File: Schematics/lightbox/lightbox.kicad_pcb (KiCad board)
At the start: 2 copper layers, 51 x 62 mm, 25 parts, among them J1 Screw_Terminal_01x04, J2 Conn_01x11_Female, J3 Conn_01x07_Female, J4 Conn_02x03_Odd_Even, Q1 IRF530, Q2 IRF530, U1 74AHCT595, U2 74HC595, U3 ATtiny85-20P, U4 LM317_TO-220

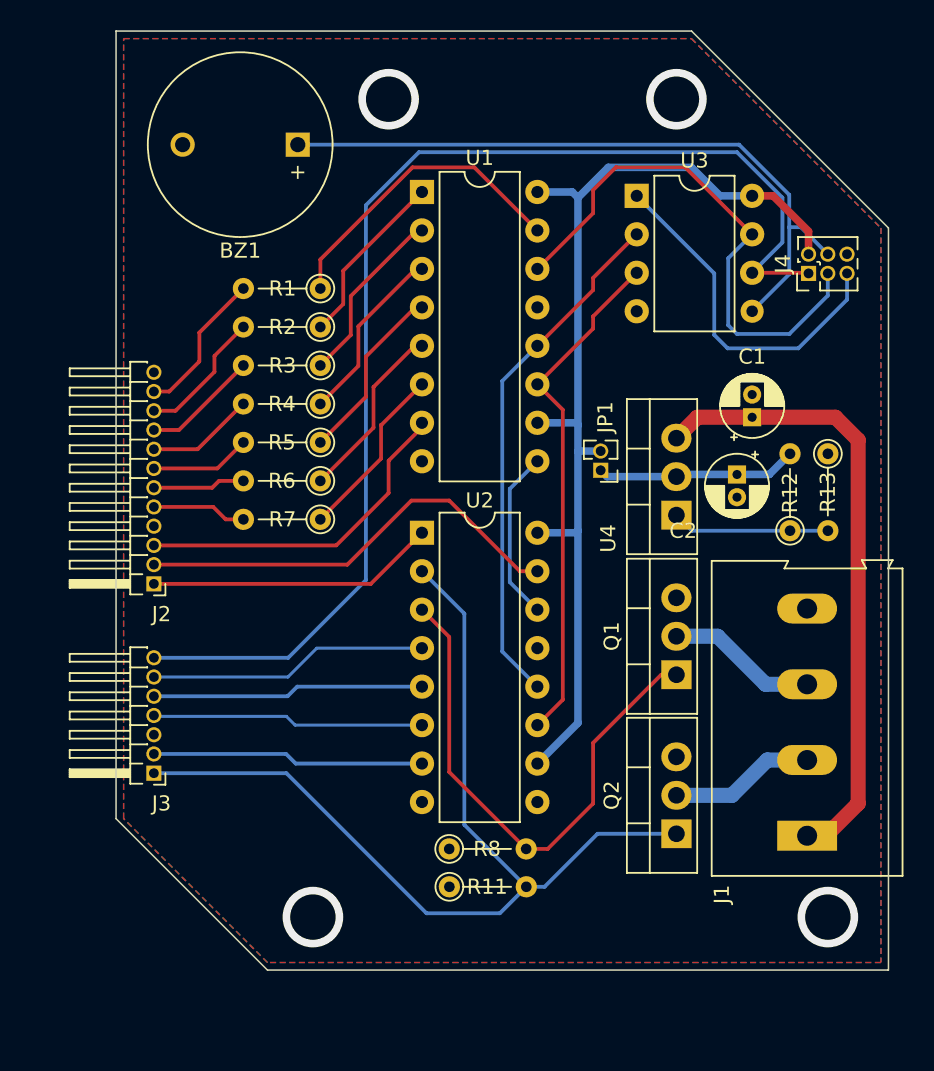
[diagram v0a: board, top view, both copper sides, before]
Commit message: Update lightbox design
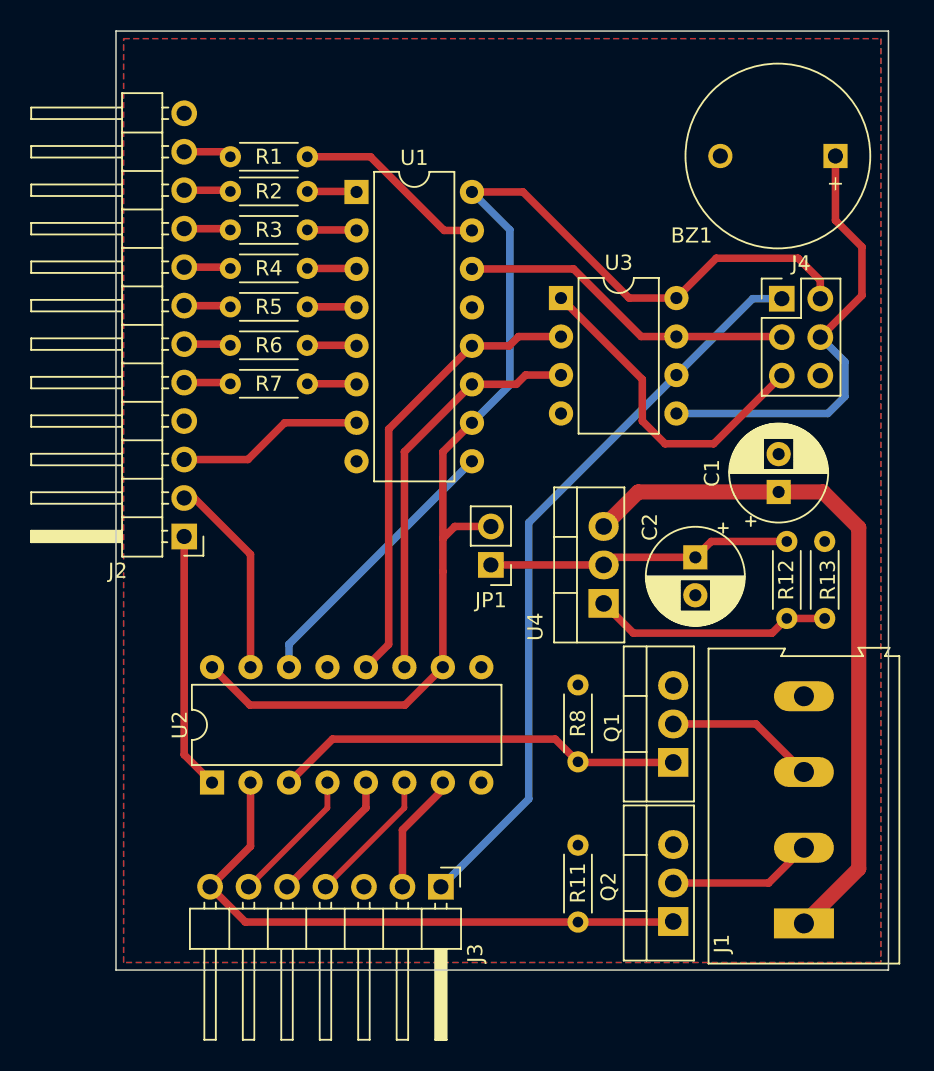
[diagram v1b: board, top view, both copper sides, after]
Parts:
- C1: value 0.1µF -> 100nF; footprint Capacitor_THT:CP_Radial_D4.0mm_P1.50mm -> Capacitor_THT:CP_Radial_D6.3mm_P2.50mm
- C2: value 10µF -> 1µF; footprint Capacitor_THT:CP_Radial_D4.0mm_P1.50mm -> Capacitor_THT:CP_Radial_D6.3mm_P2.50mm
- J2: value Conn_01x11_Female -> Conn_01x11_Pin; footprint Connector_PinHeader_1.27mm:PinHeader_1x12_P1.27mm_Horizontal -> Connector_PinHeader_2.54mm:PinHeader_1x12_P2.54mm_Horizontal
- J3: value Conn_01x07_Female -> Conn_01x07_Pin; footprint Connector_PinHeader_1.27mm:PinHeader_1x07_P1.27mm_Horizontal -> Connector_PinHeader_2.54mm:PinHeader_1x07_P2.54mm_Horizontal
- J4: footprint Connector_PinHeader_1.27mm:PinHeader_2x03_P1.27mm_Vertical -> Connector_PinHeader_2.54mm:PinHeader_2x03_P2.54mm_Vertical
- JP1: footprint Connector_PinHeader_1.27mm:PinHeader_1x02_P1.27mm_Vertical -> Connector_PinHeader_2.54mm:PinHeader_1x02_P2.54mm_Vertical
- R1, R11, R2, R3, R4, R5, R6, R7, R8: footprint Resistor_THT:R_Axial_DIN0204_L3.6mm_D1.6mm_P5.08mm_Vertical -> Resistor_THT:R_Axial_DIN0204_L3.6mm_D1.6mm_P5.08mm_Horizontal
- R12: value 100 -> 100R; footprint Resistor_THT:R_Axial_DIN0204_L3.6mm_D1.6mm_P5.08mm_Vertical -> Resistor_THT:R_Axial_DIN0204_L3.6mm_D1.6mm_P5.08mm_Horizontal
- R13: value 220 -> 220R; footprint Resistor_THT:R_Axial_DIN0204_L3.6mm_D1.6mm_P5.08mm_Vertical -> Resistor_THT:R_Axial_DIN0204_L3.6mm_D1.6mm_P5.08mm_Horizontal
- moved BZ1 35.5 mm to (170.0, 77.2)
- moved U2 21.5 mm to (128.8, 118.6), turned to 90 degrees
- moved J3 20.4 mm to (143.9, 125.5), turned to -90 degrees
- moved R8 13.8 mm to (153.0, 112.2), turned to -90 degrees
- moved JP1 9.57 mm to (147.2, 104.2)
- moved R2 8.99 mm to (135.1, 79.6)
- moved R3 8.99 mm to (135.1, 82.1)
- moved R4 8.99 mm to (135.1, 84.7)
- moved R5 8.99 mm to (135.1, 87.2)
- moved R6 8.99 mm to (135.1, 89.8)
- moved R7 8.99 mm to (135.1, 92.3)
- moved R11 8.92 mm to (153.0, 122.8), turned to -90 degrees
- moved R1 8.74 mm to (135.1, 77.3)
- moved U3 8.40 mm to (151.9, 86.6)
- moved U4 7.55 mm to (154.7, 106.8)
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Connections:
- net +3V3 renamed VCC
- J2 pad 4: /H -> unconnected-(J2-Pin_4-Pad4)
- J3 pad 1: /UVLeds -> /D_{1}
- J3 pad 7: /D_{1} -> /UVLeds
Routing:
- net /D_{1}: track 80.6 -> 49.3 mm
- net /UVLeds: track 64.2 -> 39.5 mm
- net VCC: track 67.6 -> 83.9 mm
- net /Buzzer: track 45.8 -> 30.0 mm
- net /Digit2: track 29.0 -> 13.4 mm
- net /D_{2}: track 35.7 -> 22.3 mm
- net /Digit1: track 22.5 -> 12.4 mm
- net /SW_Push_START: track 18.0 -> 7.99 mm
- net /SW_Push_-: track 18.5 -> 9.04 mm
- net /SW_Push_+: track 18.0 -> 9.04 mm
- net /SW_Push_RESET: track 18.0 -> 9.04 mm
- net Net-(U1-QF): track 12.0 -> 3.26 mm
- net Net-(U1-QE): track 12.0 -> 3.26 mm
- net Net-(U1-QD): track 11.9 -> 3.26 mm
- net Net-(U1-QC): track 11.9 -> 3.26 mm
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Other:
- outline, holes or cut-outs redrawn
